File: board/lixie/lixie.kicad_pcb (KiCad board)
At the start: 2 copper layers, 67.5 x 37.8 mm, 41 parts, among them P1 USB_OTG, U1 IS31FL3738, U2 MIC550x, U3 MAX40200, U4 STM32L073xZ

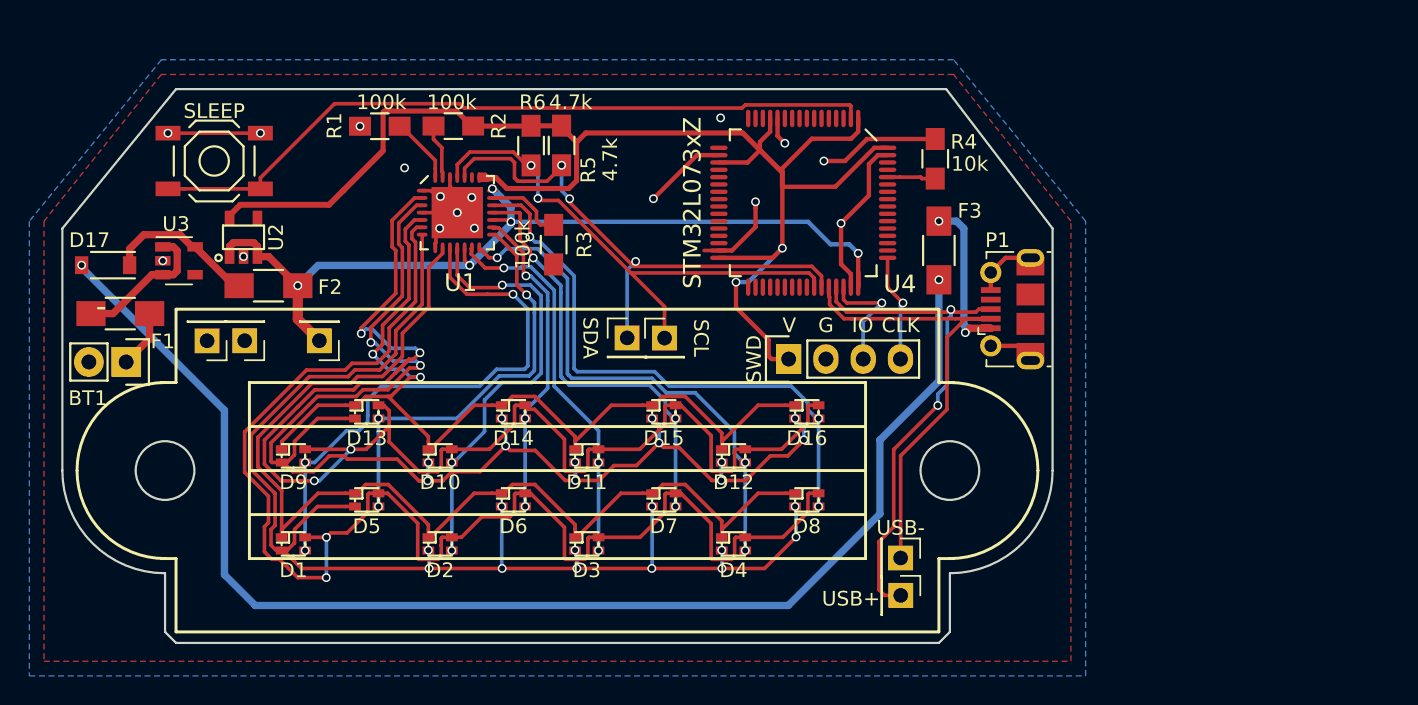
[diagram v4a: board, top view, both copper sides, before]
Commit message: apparently I routed EVERY FUCKING LED WRONG so now I gotta fix it
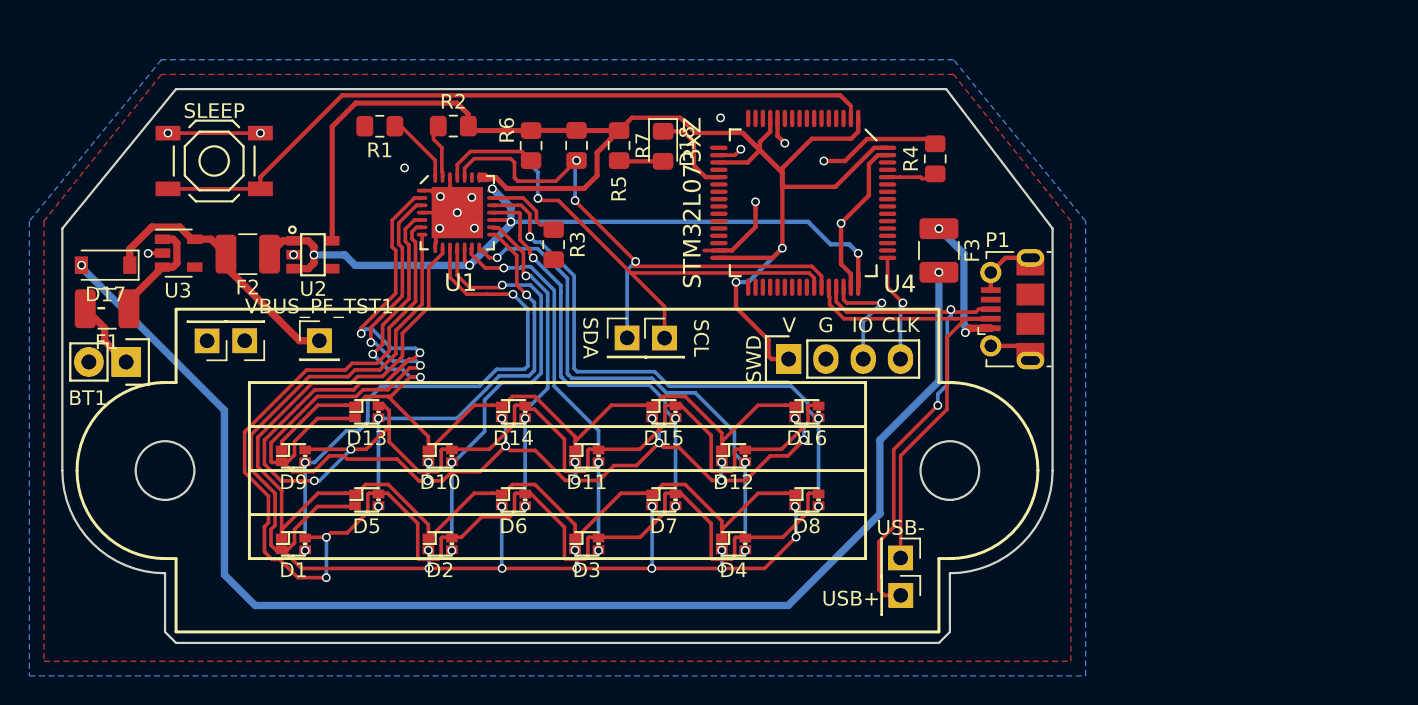
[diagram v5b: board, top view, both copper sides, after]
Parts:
- removed VBUS_TST1: TestPoint, Connector_PinHeader_2.54mm:PinHeader_1x01_P2.54mm_Vertical
- added D18: LED, LED_SMD:LED_0805_2012Metric_Pad1.15x1.40mm_HandSolder, F.Cu at (111.2, 65.9)
- added R7: R, Resistor_SMD:R_0805_2012Metric_Pad1.15x1.40mm_HandSolder, F.Cu at (108.2, 65.8)
- added VBUS_PF_TST1: TestPoint, Connector_PinHeader_2.54mm:PinHeader_1x01_P2.54mm_Vertical, F.Cu at (87.8, 79.2)
- D1, D10, D11, D12, D13, D14, D15, D16, D2, D3, D4, D5, D6, D7, D8, D9: footprint lixie:LED_ARGB_0606 -> lixie:LED_RGAB_0606
- D17: footprint Diodes_SMD:SOD-123 -> Diode_SMD:D_SOD-123
- F1, F2, F3: footprint Resistors_SMD:R_1206_HandSoldering -> Fuse:Fuse_1210_3225Metric_Pad1.42x2.65mm_HandSolder
- R1, R2, R3, R4, R5, R6: footprint Resistors_SMD:R_0805_HandSoldering -> Resistor_SMD:R_0805_2012Metric_Pad1.15x1.40mm_HandSolder
- moved U2 4.88 mm to (87.3, 73.3), turned to 0 degrees
- moved F2 2.57 mm to (82.9, 73.2)
- moved R5 1.02 mm to (105.3, 65.8)
- moved F1 0.96 mm to (73.3, 77.0), turned to 180 degrees
- moved U3 0.52 mm to (78.2, 73.2)
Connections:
- U4 pad 21: Net-(U4-Pad21) -> /CRASH_LED
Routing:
- net Net-(D17-Pad1): track 10.4 -> 18.4 mm
- net VBUS: track 61.3 -> 54.8 mm
- net /CRASH_LED: track 0.00 -> 6.03 mm
- net GND: track 57.9 -> 54.9 mm, vias 17 -> 16
- net Net-(D18-Pad2): track 0.00 -> 3.02 mm
- net Net-(F1-Pad1): track 9.55 -> 7.34 mm
- net +5V: track 12.1 -> 10.9 mm
- net +BATT: track 3.96 -> 4.80 mm
- net /SDA: track 37.9 -> 38.7 mm
- net Net-(D17-Pad2): track 90.9 -> 91.4 mm
- net /SCL: track 36.2 -> 36.4 mm, vias 2 -> 1

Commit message: kicad crashed so now I am wiring the LEDs for a fucking 3rd time
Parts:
- added JP1: Jumper_2_Open, Jumper:SolderJumper-2_P1.3mm_Open_TrianglePad1.0x1.5mm, F.Cu at (120.9, 68.9)
- D1, D10, D11, D12, D13, D14, D15, D16, D2, D3, D4, D5, D6, D7, D8, D9: value LED_RGAB -> LED_ARBG; footprint lixie:LED_RGAB_0606 -> lixie:LED_LSTD_0606
- F1, F2, F3: footprint Fuse:Fuse_1210_3225Metric_Pad1.42x2.65mm_HandSolder -> Fuse:Fuse_0805_2012Metric_Pad1.15x1.40mm_HandSolder
- R1, R2: value 100k -> 4.7k
- R4: value 10k -> 100k
- R5: value 4.7k -> 100k
- R6: value 4.7k -> R
- R7: value R -> 10k
- U2: value MIC550x -> MAX40200; footprint lixie:MIC550x -> lixie:MAX40200
- U3: value MAX40200 -> MIC550x; footprint lixie:MAX40200 -> lixie:MIC550x
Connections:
- D11 pad 1: Net-(D10-Pad1) -> Net-(D11-Pad1)
- D11 pad 3: Net-(D11-Pad3) -> Net-(D10-Pad3)
- D12 pad 1: Net-(D10-Pad1) -> Net-(D12-Pad1)
- D12 pad 3: Net-(D12-Pad3) -> Net-(D10-Pad3)
- D13 pad 1: Net-(D10-Pad1) -> Net-(D13-Pad1)
- D13 pad 3: Net-(D13-Pad3) -> Net-(D10-Pad3)
- D14 pad 1: Net-(D10-Pad1) -> Net-(D14-Pad1)
- D14 pad 3: Net-(D14-Pad3) -> Net-(D10-Pad3)
- D15 pad 1: Net-(D10-Pad1) -> Net-(D15-Pad1)
- D15 pad 3: Net-(D15-Pad3) -> Net-(D10-Pad3)
- D16 pad 1: Net-(D10-Pad1) -> Net-(D16-Pad1)
- D16 pad 3: Net-(D16-Pad3) -> Net-(D10-Pad3)
- D2 pad 1: Net-(D1-Pad1) -> Net-(D10-Pad1)
- D2 pad 3: Net-(D10-Pad3) -> Net-(D1-Pad3)
- D3 pad 1: Net-(D1-Pad1) -> Net-(D11-Pad1)
- D3 pad 3: Net-(D11-Pad3) -> Net-(D1-Pad3)
- D4 pad 1: Net-(D1-Pad1) -> Net-(D12-Pad1)
- D4 pad 3: Net-(D12-Pad3) -> Net-(D1-Pad3)
- D5 pad 1: Net-(D1-Pad1) -> Net-(D13-Pad1)
- D5 pad 3: Net-(D13-Pad3) -> Net-(D1-Pad3)
- D6 pad 1: Net-(D1-Pad1) -> Net-(D14-Pad1)
- D6 pad 3: Net-(D14-Pad3) -> Net-(D1-Pad3)
- D7 pad 1: Net-(D1-Pad1) -> Net-(D15-Pad1)
- D7 pad 3: Net-(D15-Pad3) -> Net-(D1-Pad3)
- D8 pad 1: Net-(D1-Pad1) -> Net-(D16-Pad1)
- D8 pad 3: Net-(D16-Pad3) -> Net-(D1-Pad3)
- D9 pad 1: Net-(D10-Pad1) -> Net-(D1-Pad1)
- D9 pad 3: Net-(D1-Pad3) -> Net-(D10-Pad3)
- R1 pad 1: /SDB -> +3V3
- R1 pad 2: GND -> /SDA
- R2 pad 1: /INTB -> +3V3
- R2 pad 2: +3V3 -> /SCL
- R3 pad 1: /LED_CURRENT -> /SDB
- R4 pad 1: /BOOT0 -> /INTB
- R4 pad 2: GND -> +3V3
- R5 pad 1: +3V3 -> /LED_CURRENT
- R5 pad 2: /SDA -> GND
- R6 pad 2: /SCL -> Net-(D18-Pad2)
- R7 pad 1: +3V3 -> /BOOT0
- R7 pad 2: Net-(D18-Pad2) -> GND
- U1 pad 10: Net-(D1-Pad3) -> Net-(D1-Pad1)
- U1 pad 11: Net-(D10-Pad3) -> Net-(D10-Pad1)
- U1 pad 13: Net-(D11-Pad3) -> Net-(D11-Pad1)
- U1 pad 14: Net-(D12-Pad3) -> Net-(D12-Pad1)
- U1 pad 15: Net-(D13-Pad3) -> Net-(D13-Pad1)
- U1 pad 16: Net-(D14-Pad3) -> Net-(D14-Pad1)
- U1 pad 18: Net-(D15-Pad3) -> Net-(D15-Pad1)
- U1 pad 19: Net-(D16-Pad3) -> Net-(D16-Pad1)
- U1 pad 2: Net-(D10-Pad4) -> Net-(D10-Pad3)
- U1 pad 3: Net-(D10-Pad2) -> Net-(D10-Pad4)
- U1 pad 5: Net-(D10-Pad1) -> Net-(D10-Pad2)
- U1 pad 6: Net-(D1-Pad4) -> Net-(D1-Pad3)
- U1 pad 7: Net-(D1-Pad2) -> Net-(D1-Pad4)
- U1 pad 9: Net-(D1-Pad1) -> Net-(D1-Pad2)
- U2 pad 1: VBUS -> Net-(F1-Pad1)
- U2 pad 3: VBUS -> Net-(F1-Pad1)
- U2 pad 5: +3V3 -> Net-(D17-Pad1)
- U3 pad 1: Net-(F1-Pad1) -> VBUS
- U3 pad 3: Net-(F1-Pad1) -> VBUS
- U3 pad 5: Net-(D17-Pad1) -> +3V3
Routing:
- net +3V3: track 99.2 -> 0.00 mm, vias 2 -> 0
- net Net-(D10-Pad4): track 95.3 -> 0.00 mm, vias 4 -> 0
- net Net-(D1-Pad4): track 95.0 -> 0.00 mm, vias 2 -> 0
- net Net-(D17-Pad2): track 91.4 -> 0.00 mm, vias 2 -> 0
- net Net-(D10-Pad2): track 88.0 -> 0.00 mm, vias 14 -> 0
- net Net-(D1-Pad2): track 87.8 -> 0.00 mm, vias 12 -> 0
- net Net-(D1-Pad1): track 75.4 -> 0.00 mm
- net Net-(D10-Pad1): track 64.7 -> 0.00 mm, vias 2 -> 0
- net GND: track 54.9 -> 0.00 mm, vias 16 -> 0
- net VBUS: track 54.8 -> 0.00 mm, vias 5 -> 0
- net Net-(SW1-Pad2): track 50.8 -> 0.00 mm
- net Net-(D16-Pad3): track 39.1 -> 0.00 mm, vias 3 -> 0
- net /SDA: track 38.7 -> 0.00 mm, vias 3 -> 0
- net Net-(D1-Pad3): track 36.9 -> 0.00 mm, vias 3 -> 0
- net /SCL: track 36.4 -> 0.00 mm, vias 1 -> 0
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
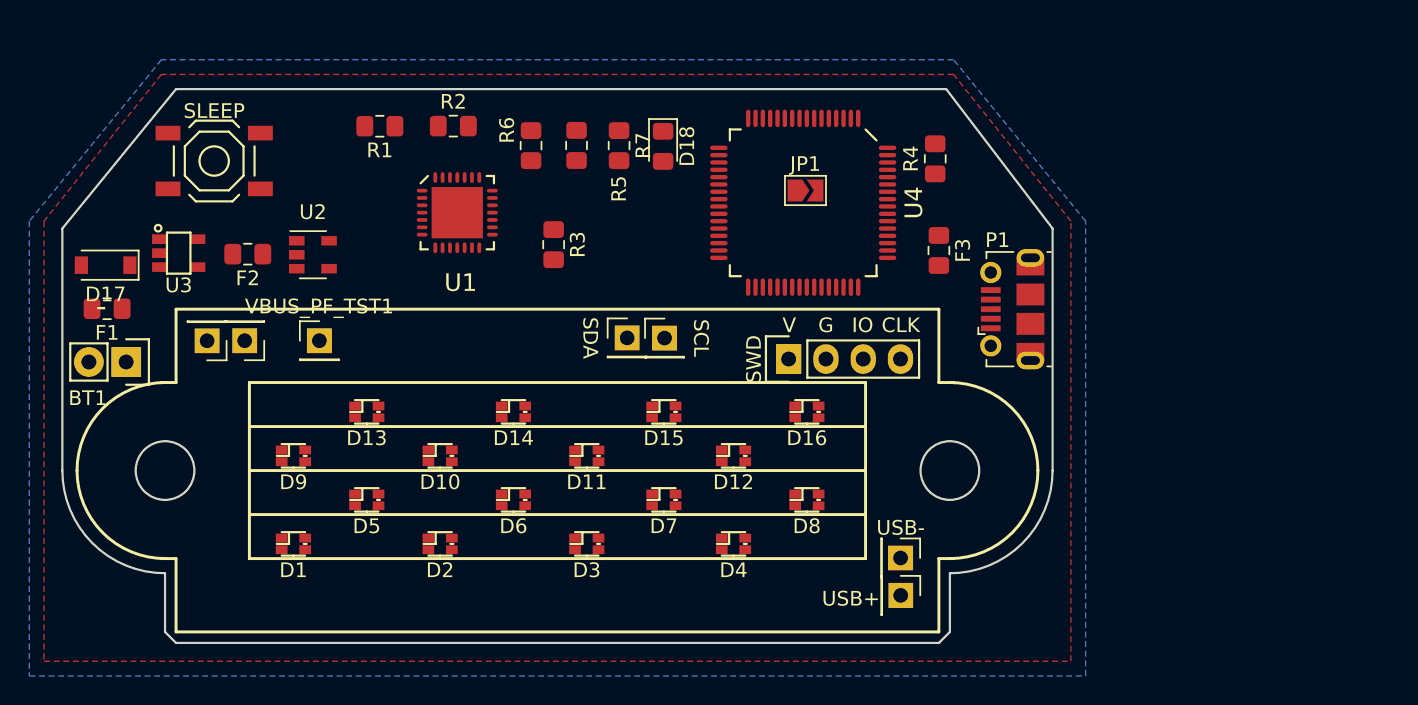
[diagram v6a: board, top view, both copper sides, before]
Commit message: made artwork, rewired the LEDs
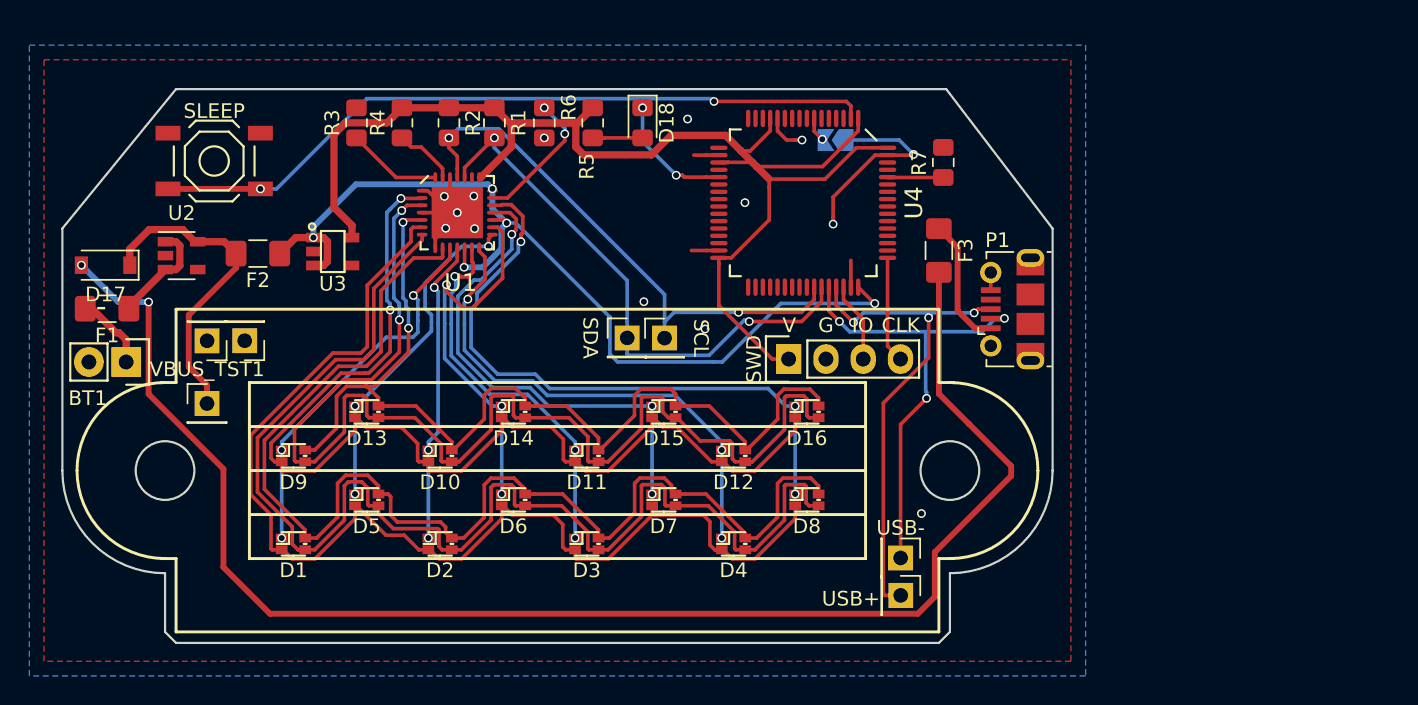
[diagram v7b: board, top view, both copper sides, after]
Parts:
- removed VBUS_PF_TST1: TestPoint, Connector_PinHeader_2.54mm:PinHeader_1x01_P2.54mm_Vertical
- added G***: LOGO, lixie:artwork, B.Cu at (103.9, 80.8)
- added VBUS_TST1: TestPoint, Connector_PinHeader_2.54mm:PinHeader_1x01_P2.54mm_Vertical, F.Cu at (80.1, 83.4)
- F1, F2, F3: footprint Fuse:Fuse_0805_2012Metric_Pad1.15x1.40mm_HandSolder -> Fuse:Fuse_1206_3216Metric_Pad1.42x1.75mm_HandSolder
- JP1: moved to B.Cu
- moved R4 36.4 mm to (93.4, 64.3)
- moved R7 22.1 mm to (130.3, 67.0), turned to 90 degrees
- moved R3 15.8 mm to (90.3, 64.3), turned to 90 degrees
- moved U3 10.5 mm to (88.7, 73.1)
- moved U2 8.95 mm to (78.4, 73.3)
- moved R1 7.81 mm to (99.7, 64.3), turned to 270 degrees
- moved R6 4.48 mm to (106.4, 64.3)
- moved JP1 4.01 mm to (123.0, 65.5), turned to 180 degrees
- moved R5 2.69 mm to (103.1, 64.3)
- moved D18 2.13 mm to (109.8, 64.3)
- moved F2 0.69 mm to (83.6, 73.2)
- moved R2 0.37 mm to (96.6, 64.3), turned to 270 degrees
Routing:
- net Net-(D17-Pad2): track 0.00 -> 102.4 mm, vias 0 -> 2
- net +3V3: track 0.00 -> 95.1 mm
- net Net-(D1-Pad4): track 0.00 -> 87.7 mm
- net Net-(D1-Pad2): track 0.00 -> 83.4 mm
- net Net-(D10-Pad4): track 0.00 -> 82.5 mm, vias 0 -> 2
- net Net-(D1-Pad3): track 0.00 -> 79.2 mm
- net Net-(D10-Pad3): track 0.00 -> 74.8 mm, vias 0 -> 2
- net Net-(D10-Pad2): track 0.00 -> 68.6 mm, vias 0 -> 2
- net VBUS: track 0.00 -> 64.5 mm, vias 0 -> 5
- net Net-(SW1-Pad2): track 0.00 -> 50.2 mm, vias 0 -> 2
- net Net-(D16-Pad1): track 0.00 -> 42.6 mm, vias 0 -> 3
- net /SDA: track 0.00 -> 37.9 mm, vias 0 -> 2
- net /SCL: track 0.00 -> 37.2 mm, vias 0 -> 3
- net Net-(D12-Pad1): track 0.00 -> 34.4 mm, vias 0 -> 3
- net /USB_DP: track 0.00 -> 34.4 mm, vias 0 -> 3
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
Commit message: got the first puzzle done
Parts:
- added REF**: Fiducial_0.75mm_Mask1.5mm, lixie:Fiducial_0.75mm_Mask1.5mm, F.Cu at (78.5, 98.4)
- added REF**: Fiducial_0.75mm_Mask1.5mm, lixie:Fiducial_0.75mm_Mask1.5mm, F.Cu at (129.4, 98.5)
- added REF**: Fiducial_0.75mm_Mask1.5mm, lixie:Fiducial_0.75mm_Mask1.5mm, F.Cu at (129.8, 63.4)
- added REF**: Fiducial_0.75mm_Mask1.5mm, lixie:Fiducial_0.75mm_Mask1.5mm, F.Cu at (78.5, 63.1)
- renumbered SLEEP to SLEEP...
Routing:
- net Net-(D17-Pad2): track 102.4 -> 101.5 mm
- net GND: vias 14 -> 16
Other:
- board text added: "Crash!"
- board text added: "GND"
- board text added: "VBUS"
